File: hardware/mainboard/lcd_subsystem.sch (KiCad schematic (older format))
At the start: 10 parts, among them J2 WP7B-S040VA1-R6000, U1 TPS65132

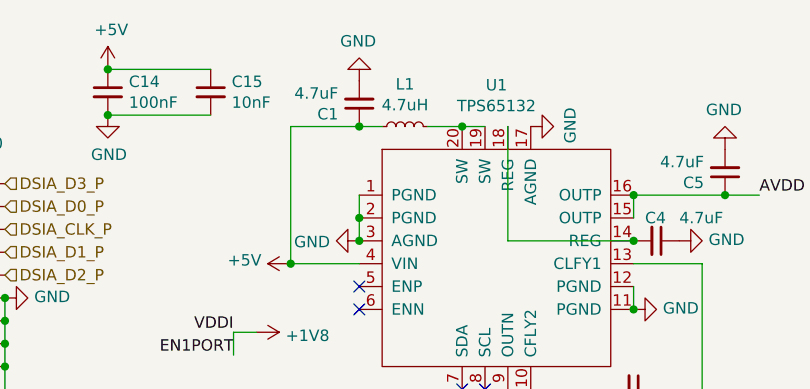
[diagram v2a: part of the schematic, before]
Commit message: footprints assigned, ready to begin pcb design
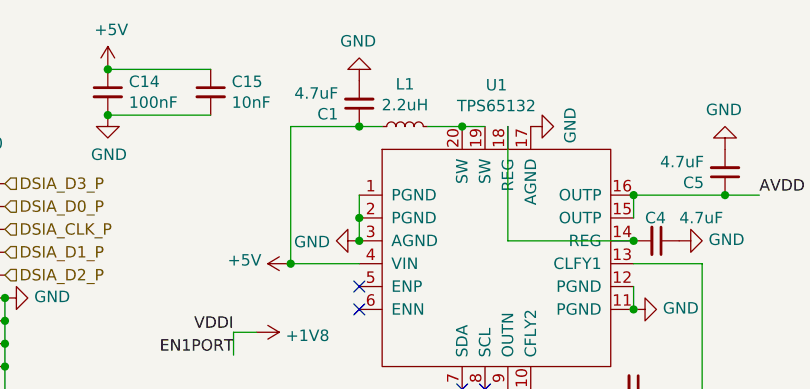
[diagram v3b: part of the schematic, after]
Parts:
- C1, C14, C15, C2, C3, C4, C5: footprint (none) -> Capacitor_SMD:C_0603_1608Metric_Pad1.08x0.95mm_HandSolder
- J2: footprint JAE_WP7B-S040VA1-R6000 -> mainboard:JAE_WP7B-S040VA1-R6000
- L1: value 4.7uH -> 2.2uH; footprint (none) -> Inductor_SMD:L_0805_2012Metric_Pad1.15x1.40mm_HandSolder
- U1: footprint (none) -> mainboard:TPS65132WRVCT
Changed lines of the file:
@@
 F 0 "J2" H 4750 5717 50  0000 C CNN
 F 1 "WP7B-S040VA1-R6000" H 4750 5626 50  0000 C CNN
-F 2 "JAE_WP7B-S040VA1-R6000" H 4750 4450 50  0001 L BNN
+F 2 "mainboard:JAE_WP7B-S040VA1-R6000" H 4750 4450 50  0001 L BNN
 F 3 "Manufacturer Recommendations" H 4750 4450 50  0001 L BNN
 F 4 "JAE ELECTRONICS" H 4750 4450 50  0001 L BNN "Field4"
@@
 AR Path="/5FA3B5FC/5F877EFB" Ref="#PWR?"  Part="1"
 AR Path="/5FA75E62/5F877EFB" Ref="#PWR0197"  Part="1"
-F 0 "#PWR0197" H 4350 5300 50  0001 C CNN
+F 0 "#PWR0189" H 4350 5300 50  0001 C CNN
 F 1 "GND" V 4355 5422 50  0000 R CNN
 F 2 "" H 4350 5550 50  0001 C CNN
@@
 AR Path="/5FA3B5FC/5F87EF2E" Ref="#PWR?"  Part="1"
 AR Path="/5FA75E62/5F87EF2E" Ref="#PWR0198"  Part="1"
-F 0 "#PWR0198" H 4350 4400 50  0001 C CNN
+F 0 "#PWR0190" H 4350 4400 50  0001 C CNN
 F 1 "GND" V 4355 4522 50  0000 R CNN
 F 2 "" H 4350 4650 50  0001 C CNN
@@
 AR Path="/5FA3B5FC/5F87F823" Ref="#PWR?"  Part="1"
 AR Path="/5FA75E62/5F87F823" Ref="#PWR0199"  Part="1"
-F 0 "#PWR0199" H 5150 4400 50  0001 C CNN
+F 0 "#PWR0191" H 5150 4400 50  0001 C CNN
 F 1 "GND" V 5155 4522 50  0000 R CNN
 F 2 "" H 5150 4650 50  0001 C CNN
@@
 AR Path="/5FA3B5FC/5F87FB91" Ref="#PWR?"  Part="1"
 AR Path="/5FA75E62/5F87FB91" Ref="#PWR0200"  Part="1"
-F 0 "#PWR0200" H 4350 4500 50  0001 C CNN
+F 0 "#PWR0192" H 4350 4500 50  0001 C CNN
 F 1 "GND" V 4355 4622 50  0000 R CNN
 F 2 "" H 4350 4750 50  0001 C CNN
@@
 AR Path="/5FA3B5FC/5F87FE21" Ref="#PWR?"  Part="1"
 AR Path="/5FA75E62/5F87FE21" Ref="#PWR0201"  Part="1"
-F 0 "#PWR0201" H 5150 4500 50  0001 C CNN
+F 0 "#PWR0193" H 5150 4500 50  0001 C CNN
 F 1 "GND" V 5155 4622 50  0000 R CNN
 F 2 "" H 5150 4750 50  0001 C CNN
@@
 AR Path="/5FA3B5FC/5F882259" Ref="#PWR?"  Part="1"
 AR Path="/5FA75E62/5F882259" Ref="#PWR0202"  Part="1"
-F 0 "#PWR0202" H 4350 4800 50  0001 C CNN
+F 0 "#PWR0194" H 4350 4800 50  0001 C CNN
 F 1 "GND" V 4355 4922 50  0000 R CNN
 F 2 "" H 4350 5050 50  0001 C CNN
@@
 AR Path="/5FA3B5FC/5F8836D9" Ref="#PWR?"  Part="1"
 AR Path="/5FA75E62/5F8836D9" Ref="#PWR0203"  Part="1"
-F 0 "#PWR0203" H 5150 4800 50  0001 C CNN
+F 0 "#PWR0195" H 5150 4800 50  0001 C CNN
 F 1 "GND" V 5155 4922 50  0000 R CNN
 F 2 "" H 5150 5050 50  0001 C CNN
@@
 AR Path="/5FA3B5FC/5F883A64" Ref="#PWR?"  Part="1"
 AR Path="/5FA75E62/5F883A64" Ref="#PWR0204"  Part="1"
-F 0 "#PWR0204" H 4350 4900 50  0001 C CNN
+F 0 "#PWR0196" H 4350 4900 50  0001 C CNN
 F 1 "GND" V 4355 5022 50  0000 R CNN
 F 2 "" H 4350 5150 50  0001 C CNN
@@
 AR Path="/5FA3B5FC/5F8A694C" Ref="#PWR?"  Part="1"
 AR Path="/5FA75E62/5F8A694C" Ref="#PWR0208"  Part="1"
-F 0 "#PWR0208" H 6250 3950 50  0001 C CNN
+F 0 "#PWR0205" H 6250 3950 50  0001 C CNN
 F 1 "+1V8" V 6265 4228 50  0000 L CNN
 F 2 "" H 6250 4100 50  0001 C CNN
@@
 AR Path="/5FA3B5FC/5F8B4999" Ref="#PWR?"  Part="1"
 AR Path="/5FA75E62/5F8B4999" Ref="#PWR0209"  Part="1"
-F 0 "#PWR0209" H 5150 3700 50  0001 C CNN
+F 0 "#PWR0206" H 5150 3700 50  0001 C CNN
 F 1 "GND" V 5155 3822 50  0000 R CNN
 F 2 "" H 5150 3950 50  0001 C CNN
@@
 AR Path="/5FA3B5FC/5F8B4E7C" Ref="#PWR?"  Part="1"
 AR Path="/5FA75E62/5F8B4E7C" Ref="#PWR0210"  Part="1"
-F 0 "#PWR0210" H 4350 3700 50  0001 C CNN
+F 0 "#PWR0207" H 4350 3700 50  0001 C CNN
 F 1 "GND" V 4355 3822 50  0000 R CNN
 F 2 "" H 4350 3950 50  0001 C CNN
@@
 AR Path="/5FA3B5FC/5F8CFB2D" Ref="#PWR?"  Part="1"
 AR Path="/5FA75E62/5F8CFB2D" Ref="#PWR0219"  Part="1"
-F 0 "#PWR0219" H 6700 3450 50  0001 C CNN
+F 0 "#PWR0212" H 6700 3450 50  0001 C CNN
 F 1 "GND" V 6705 3572 50  0000 R CNN
 F 2 "" H 6700 3700 50  0001 C CNN
@@
 AR Path="/5FA3B5FC/5F8D004B" Ref="#PWR?"  Part="1"
 AR Path="/5FA75E62/5F8D004B" Ref="#PWR0220"  Part="1"
-F 0 "#PWR0220" H 7900 3750 50  0001 C CNN
+F 0 "#PWR0213" H 7900 3750 50  0001 C CNN
 F 1 "GND" V 7905 3872 50  0000 R CNN
 F 2 "" H 7900 4000 50  0001 C CNN
@@
 AR Path="/5FA3B5FC/5F8EE799" Ref="#PWR?"  Part="1"
 AR Path="/5FA75E62/5F8EE799" Ref="#PWR0221"  Part="1"
-F 0 "#PWR0221" H 8300 3050 50  0001 C CNN
+F 0 "#PWR0214" H 8300 3050 50  0001 C CNN
 F 1 "GND" H 8305 3127 50  0000 C CNN
 F 2 "" H 8300 3300 50  0001 C CNN
@@
 F 0 "C2" H 7442 4696 50  0000 L CNN
 F 1 "4.7uF" H 7442 4605 50  0000 L CNN
-F 2 "" H 7350 4650 50  0001 C CNN
+F 2 "Capacitor_SMD:C_0603_1608Metric_Pad1.08x0.95mm_HandSolder" H 7350 4650 50  0001 C CNN
 F 3 "~" H 7350 4650 50  0001 C CNN
 	1    7350 4650
@@
 AR Path="/5FA3B5FC/5F8F28C5" Ref="#PWR?"  Part="1"
 AR Path="/5FA75E62/5F8F28C5" Ref="#PWR0222"  Part="1"
-F 0 "#PWR0222" H 7350 4500 50  0001 C CNN
+F 0 "#PWR0215" H 7350 4500 50  0001 C CNN
 F 1 "GND" H 7355 4577 50  0000 C CNN
 F 2 "" H 7350 4750 50  0001 C CNN
@@
 F 0 "C5" H 8392 3446 50  0000 L CNN
 F 1 "4.7uF" H 8392 3355 50  0000 L CNN
-F 2 "" H 8300 3400 50  0001 C CNN
+F 2 "Capacitor_SMD:C_0603_1608Metric_Pad1.08x0.95mm_HandSolder" H 8300 3400 50  0001 C CNN
 F 3 "~" H 8300 3400 50  0001 C CNN
 	1    8300 3400
@@
 F 0 "C4" V 7900 3650 50  0000 L CNN
 F 1 "4.7uF" V 7900 3800 50  0000 L CNN
-F 2 "" H 8000 3700 50  0001 C CNN
+F 2 "Capacitor_SMD:C_0603_1608Metric_Pad1.08x0.95mm_HandSolder" H 8000 3700 50  0001 C CNN
 F 3 "~" H 8000 3700 50  0001 C CNN
 	1    8000 3700
@@
 AR Path="/5FA3B5FC/5F8FEBB7" Ref="#PWR?"  Part="1"
 AR Path="/5FA75E62/5F8FEBB7" Ref="#PWR0223"  Part="1"
-F 0 "#PWR0223" H 8100 3450 50  0001 C CNN
+F 0 "#PWR0216" H 8100 3450 50  0001 C CNN
 F 1 "GND" V 8105 3572 50  0000 R CNN
 F 2 "" H 8100 3700 50  0001 C CNN
@@
 F 0 "C3" H 7992 4396 50  0000 L CNN
 F 1 "2.2uF" H 7992 4305 50  0000 L CNN
-F 2 "" H 7900 4350 50  0001 C CNN
+F 2 "Capacitor_SMD:C_0603_1608Metric_Pad1.08x0.95mm_HandSolder" H 7900 4350 50  0001 C CNN
 F 3 "~" H 7900 4350 50  0001 C CNN
 	1    7900 4350
@@
 AR Path="/5FA75E62/5F908EBB" Ref="L2"  Part="1"
 F 0 "L1" V 7085 3200 50  0000 C CNN
-F 1 "4.7uH" V 6994 3200 50  0000 C CNN
-F 2 "" H 6900 3200 50  0001 C CNN
+F 1 "2.2uH" V 6994 3200 50  0000 C CNN
+F 2 "Inductor_SMD:L_0805_2012Metric_Pad1.15x1.40mm_HandSolder" H 6900 3200 50  0001 C CNN
 F 3 "~" H 6900 3200 50  0001 C CNN
 	1    6900 3200
@@
 AR Path="/5FA3B5FC/5F90F39D" Ref="#PWR?"  Part="1"
 AR Path="/5FA75E62/5F90F39D" Ref="#PWR0224"  Part="1"
-F 0 "#PWR0224" H 6700 2750 50  0001 C CNN
+F 0 "#PWR0217" H 6700 2750 50  0001 C CNN
 F 1 "GND" H 6705 2827 50  0000 C CNN
 F 2 "" H 6700 3000 50  0001 C CNN
@@
 F 0 "C1" H 6792 3146 50  0000 L CNN
 F 1 "4.7uF" H 6792 3055 50  0000 L CNN
-F 2 "" H 6700 3100 50  0001 C CNN
+F 2 "Capacitor_SMD:C_0603_1608Metric_Pad1.08x0.95mm_HandSolder" H 6700 3100 50  0001 C CNN
 F 3 "~" H 6700 3100 50  0001 C CNN
 	1    6700 3100
@@
 AR Path="/5FA3B5FC/5F916340" Ref="#PWR?"  Part="1"
 AR Path="/5FA75E62/5F916340" Ref="#PWR0225"  Part="1"
-F 0 "#PWR0225" H 7450 2950 50  0001 C CNN
+F 0 "#PWR0218" H 7450 2950 50  0001 C CNN
 F 1 "GND" H 7455 3027 50  0000 C CNN
 F 2 "" H 7450 3200 50  0001 C CNN
@@
 F 0 "U1" H 7300 4381 50  0000 C CNN
 F 1 "TPS65132" H 7300 4290 50  0000 C CNN
-F 2 "" H 7300 3650 50  0001 C CNN
+F 2 "mainboard:TPS65132WRVCT" H 7300 3650 50  0001 C CNN
 F 3 "" H 7300 3650 50  0001 C CNN
 	1    7300 3700
@@
 AR Path="/5F86493C/6021D52E" Ref="#PWR0262"  Part="1"
 AR Path="/5FA75E62/6021D52E" Ref="#PWR0265"  Part="1"
-F 0 "#PWR0265" H 6400 3650 50  0001 C CNN
+F 0 "#PWR0262" H 6400 3650 50  0001 C CNN
 F 1 "+5V" V 6415 3928 50  0000 L CNN
 F 2 "" H 6400 3800 50  0001 C CNN
@@
 F 0 "C14" H 5692 3096 50  0000 L CNN
 F 1 "100nF" H 5692 3005 50  0000 L CNN
-F 2 "" H 5600 3050 50  0001 C CNN
+F 2 "Capacitor_SMD:C_0603_1608Metric_Pad1.08x0.95mm_HandSolder" H 5600 3050 50  0001 C CNN
 F 3 "~" H 5600 3050 50  0001 C CNN
 	1    5600 3050
@@
 AR Path="/5F86493C/6021FA8C" Ref="#PWR0263"  Part="1"
 AR Path="/5FA75E62/6021FA8C" Ref="#PWR0266"  Part="1"
-F 0 "#PWR0266" H 5600 2900 50  0001 C CNN
+F 0 "#PWR0263" H 5600 2900 50  0001 C CNN
 F 1 "GND" H 5605 2977 50  0000 C CNN
 F 2 "" H 5600 3150 50  0001 C CNN
@@
 AR Path="/5F86493C/6021FEAB" Ref="#PWR0264"  Part="1"
 AR Path="/5FA75E62/6021FEAB" Ref="#PWR0267"  Part="1"
-F 0 "#PWR0267" H 5600 2800 50  0001 C CNN
+F 0 "#PWR0264" H 5600 2800 50  0001 C CNN
 F 1 "+5V" H 5615 3123 50  0000 C CNN
 F 2 "" H 5600 2950 50  0001 C CNN
@@
 F 0 "C15" H 6142 3096 50  0000 L CNN
 F 1 "10nF" H 6142 3005 50  0000 L CNN
-F 2 "" H 6050 3050 50  0001 C CNN
+F 2 "Capacitor_SMD:C_0603_1608Metric_Pad1.08x0.95mm_HandSolder" H 6050 3050 50  0001 C CNN
 F 3 "~" H 6050 3050 50  0001 C CNN
 	1    6050 3050

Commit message: mipi done, power almost done
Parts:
- C1, C14, C15, C2, C3, C4, C5: footprint Capacitor_SMD:C_0603_1608Metric_Pad1.08x0.95mm_HandSolder -> Capacitor_SMD:C_0402_1005Metric_Pad0.74x0.62mm_HandSolder
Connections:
- net +5V renamed +3V3

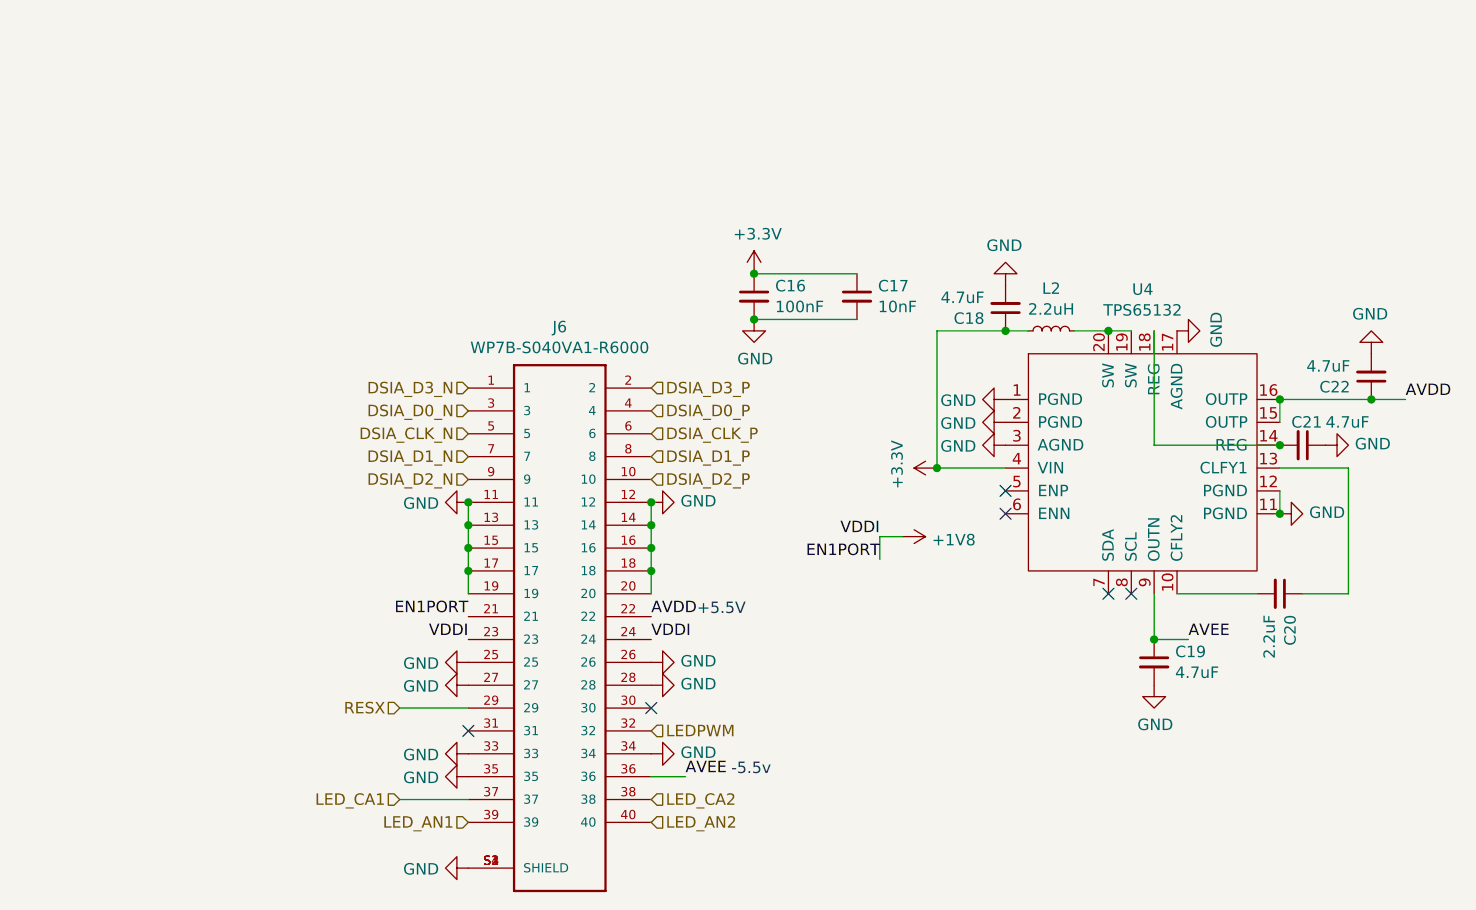
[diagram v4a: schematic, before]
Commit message: 0.1 routing done, will merge after cleaning up silkscreen
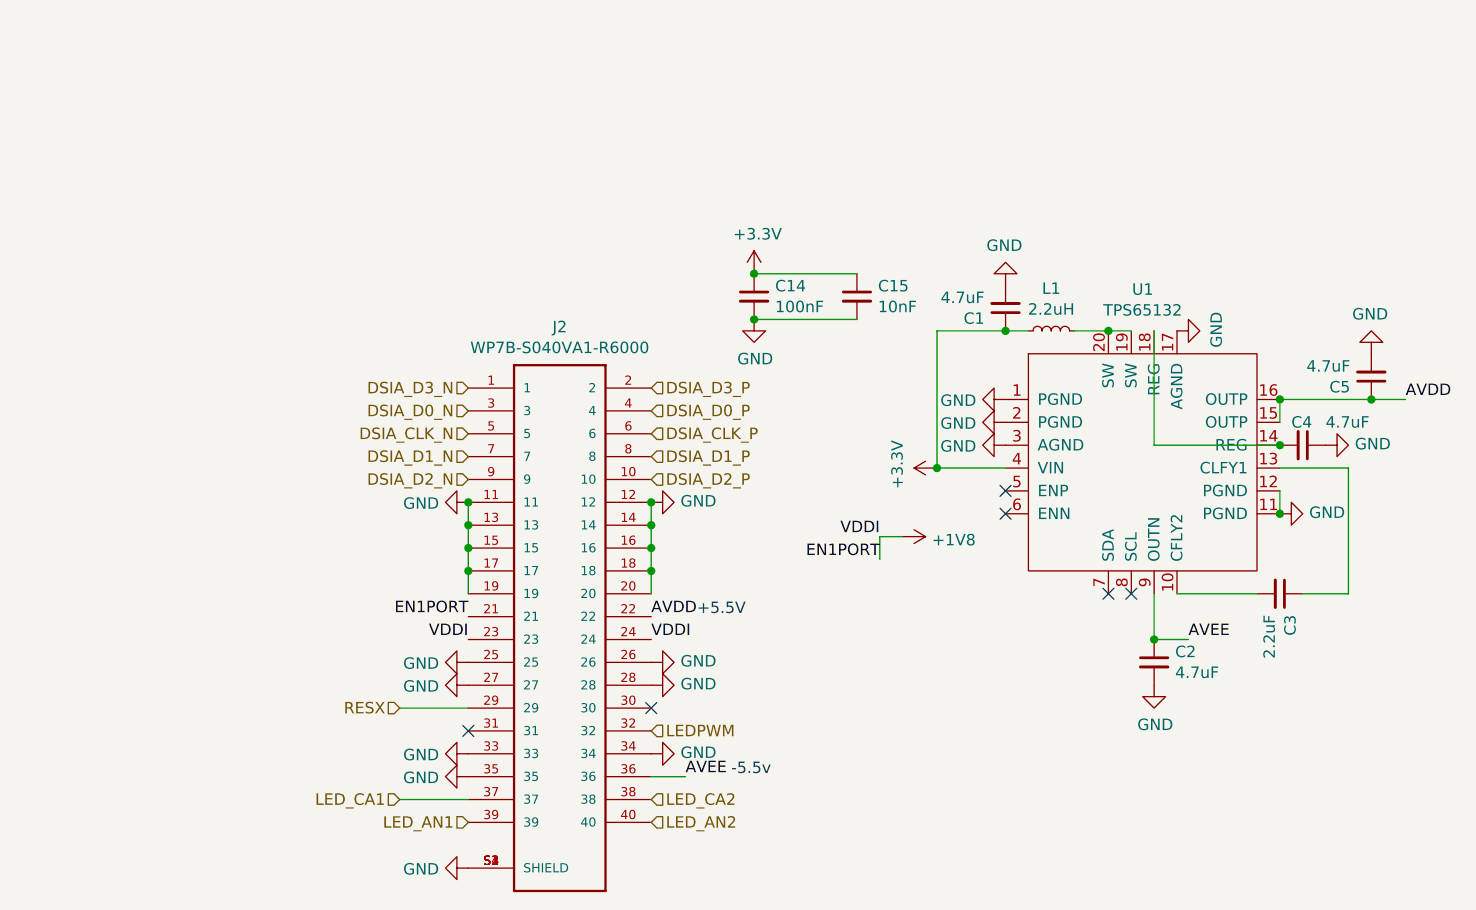
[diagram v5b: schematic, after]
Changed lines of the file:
@@
 $Descr A4 11693 8268
 encoding utf-8
-Sheet 3 3
+Sheet 2 3
 Title ""
 Date ""
@@
 AR Path="/5FA3B5FC/5FA221C8" Ref="J?"  Part="1"
 AR Path="/5FA75E62/5FA221C8" Ref="J6"  Part="1"
-F 0 "J6" H 4750 5717 50  0000 C CNN
+F 0 "J2" H 4750 5717 50  0000 C CNN
 F 1 "WP7B-S040VA1-R6000" H 4750 5626 50  0000 C CNN
 F 2 "mainboard:JAE_WP7B-S040VA1-R6000" H 4750 4450 50  0001 L BNN
@@
 AR Path="/5FA3B5FC/5F8F28BE" Ref="C?"  Part="1"
 AR Path="/5FA75E62/5F8F28BE" Ref="C19"  Part="1"
-F 0 "C19" H 7442 4696 50  0000 L CNN
+F 0 "C2" H 7442 4696 50  0000 L CNN
 F 1 "4.7uF" H 7442 4605 50  0000 L CNN
 F 2 "Capacitor_SMD:C_0402_1005Metric_Pad0.74x0.62mm_HandSolder" H 7350 4650 50  0001 C CNN
@@
 AR Path="/5FA3B5FC/5F8D1308" Ref="C?"  Part="1"
 AR Path="/5FA75E62/5F8D1308" Ref="C22"  Part="1"
-F 0 "C22" H 8392 3446 50  0000 L CNN
+F 0 "C5" H 8392 3446 50  0000 L CNN
 F 1 "4.7uF" H 8392 3355 50  0000 L CNN
 F 2 "Capacitor_SMD:C_0402_1005Metric_Pad0.74x0.62mm_HandSolder" H 8300 3400 50  0001 C CNN
@@
 AR Path="/5FA3B5FC/5F8FE2CF" Ref="C?"  Part="1"
 AR Path="/5FA75E62/5F8FE2CF" Ref="C21"  Part="1"
-F 0 "C21" V 7900 3650 50  0000 L CNN
+F 0 "C4" V 7900 3650 50  0000 L CNN
 F 1 "4.7uF" V 7900 3800 50  0000 L CNN
 F 2 "Capacitor_SMD:C_0402_1005Metric_Pad0.74x0.62mm_HandSolder" H 8000 3700 50  0001 C CNN
@@
 AR Path="/5FA3B5FC/5F901A08" Ref="C?"  Part="1"
 AR Path="/5FA75E62/5F901A08" Ref="C20"  Part="1"
-F 0 "C20" H 7992 4396 50  0000 L CNN
+F 0 "C3" H 7992 4396 50  0000 L CNN
 F 1 "2.2uF" H 7992 4305 50  0000 L CNN
 F 2 "Capacitor_SMD:C_0402_1005Metric_Pad0.74x0.62mm_HandSolder" H 7900 4350 50  0001 C CNN
@@
 AR Path="/5FA3B5FC/5F908EBB" Ref="L?"  Part="1"
 AR Path="/5FA75E62/5F908EBB" Ref="L2"  Part="1"
-F 0 "L2" V 7085 3200 50  0000 C CNN
+F 0 "L1" V 7085 3200 50  0000 C CNN
 F 1 "2.2uH" V 6994 3200 50  0000 C CNN
 F 2 "Inductor_SMD:L_0805_2012Metric_Pad1.15x1.40mm_HandSolder" H 6900 3200 50  0001 C CNN
@@
 AR Path="/5FA3B5FC/5F90F3A3" Ref="C?"  Part="1"
 AR Path="/5FA75E62/5F90F3A3" Ref="C18"  Part="1"
-F 0 "C18" H 6792 3146 50  0000 L CNN
+F 0 "C1" H 6792 3146 50  0000 L CNN
 F 1 "4.7uF" H 6792 3055 50  0000 L CNN
 F 2 "Capacitor_SMD:C_0402_1005Metric_Pad0.74x0.62mm_HandSolder" H 6700 3100 50  0001 C CNN
@@
 AR Path="/5FA3B5FC/5F8CA6D9" Ref="U?"  Part="1"
 AR Path="/5FA75E62/5F8CA6D9" Ref="U4"  Part="1"
-F 0 "U4" H 7300 4381 50  0000 C CNN
+F 0 "U1" H 7300 4381 50  0000 C CNN
 F 1 "TPS65132" H 7300 4290 50  0000 C CNN
 F 2 "mainboard:TPS65132WRVCT" H 7300 3650 50  0001 C CNN
@@
 AR Path="/5F86493C/6021F152" Ref="C14"  Part="1"
 AR Path="/5FA75E62/6021F152" Ref="C16"  Part="1"
-F 0 "C16" H 5692 3096 50  0000 L CNN
+F 0 "C14" H 5692 3096 50  0000 L CNN
 F 1 "100nF" H 5692 3005 50  0000 L CNN
 F 2 "Capacitor_SMD:C_0402_1005Metric_Pad0.74x0.62mm_HandSolder" H 5600 3050 50  0001 C CNN
@@
 AR Path="/5F86493C/602249E9" Ref="C15"  Part="1"
 AR Path="/5FA75E62/602249E9" Ref="C17"  Part="1"
-F 0 "C17" H 6142 3096 50  0000 L CNN
+F 0 "C15" H 6142 3096 50  0000 L CNN
 F 1 "10nF" H 6142 3005 50  0000 L CNN
 F 2 "Capacitor_SMD:C_0402_1005Metric_Pad0.74x0.62mm_HandSolder" H 6050 3050 50  0001 C CNN
@@
 Connection ~ 6400 3800
 $Comp
-L power:GND #PWR?
+L power:GND #PWR0274
 U 1 1 5F98BA7B
 P 6700 3600
-AR Path="/5F86493C/5F98BA7B" Ref="#PWR?"  Part="1"
+AR Path="/5F86493C/5F98BA7B" Ref="#PWR0274"  Part="1"
 AR Path="/5F89AA7A/5F98BA7B" Ref="#PWR?"  Part="1"
 AR Path="/5FA3B5FC/5F98BA7B" Ref="#PWR?"  Part="1"
-AR Path="/5FA75E62/5F98BA7B" Ref="#PWR?"  Part="1"
-F 0 "#PWR?" H 6700 3350 50  0001 C CNN
+AR Path="/5FA75E62/5F98BA7B" Ref="#PWR0276"  Part="1"
+F 0 "#PWR0276" H 6700 3350 50  0001 C CNN
 F 1 "GND" V 6705 3472 50  0000 R CNN
 F 2 "" H 6700 3600 50  0001 C CNN
@@
 $EndComp
 $Comp
-L power:GND #PWR?
+L power:GND #PWR0275
 U 1 1 5F98C057
 P 6700 3500
-AR Path="/5F86493C/5F98C057" Ref="#PWR?"  Part="1"
+AR Path="/5F86493C/5F98C057" Ref="#PWR0275"  Part="1"
 AR Path="/5F89AA7A/5F98C057" Ref="#PWR?"  Part="1"
 AR Path="/5FA3B5FC/5F98C057" Ref="#PWR?"  Part="1"
-AR Path="/5FA75E62/5F98C057" Ref="#PWR?"  Part="1"
-F 0 "#PWR?" H 6700 3250 50  0001 C CNN
+AR Path="/5FA75E62/5F98C057" Ref="#PWR0277"  Part="1"
+F 0 "#PWR0277" H 6700 3250 50  0001 C CNN
 F 1 "GND" V 6705 3372 50  0000 R CNN
 F 2 "" H 6700 3500 50  0001 C CNN
